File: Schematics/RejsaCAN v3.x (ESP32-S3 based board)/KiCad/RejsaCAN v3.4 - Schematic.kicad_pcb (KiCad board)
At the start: 4 copper layers, 63 x 49.5 mm, 86 parts, among them J1 Micro-Fit 3.0 4P R/A, J2 U.FL, J3 JST-XH 4P LTE, Q1 SS8050, U1 ESP32-S3-WROOM-1(N16R8), U2 SN65HVD230DR, U3 ME2807A33M3G, U4 LMR14006XDDCR, U5 MT9700, U6 CPC1018N, U7 LG290P03AAMD, U8 AP2112K-3.3

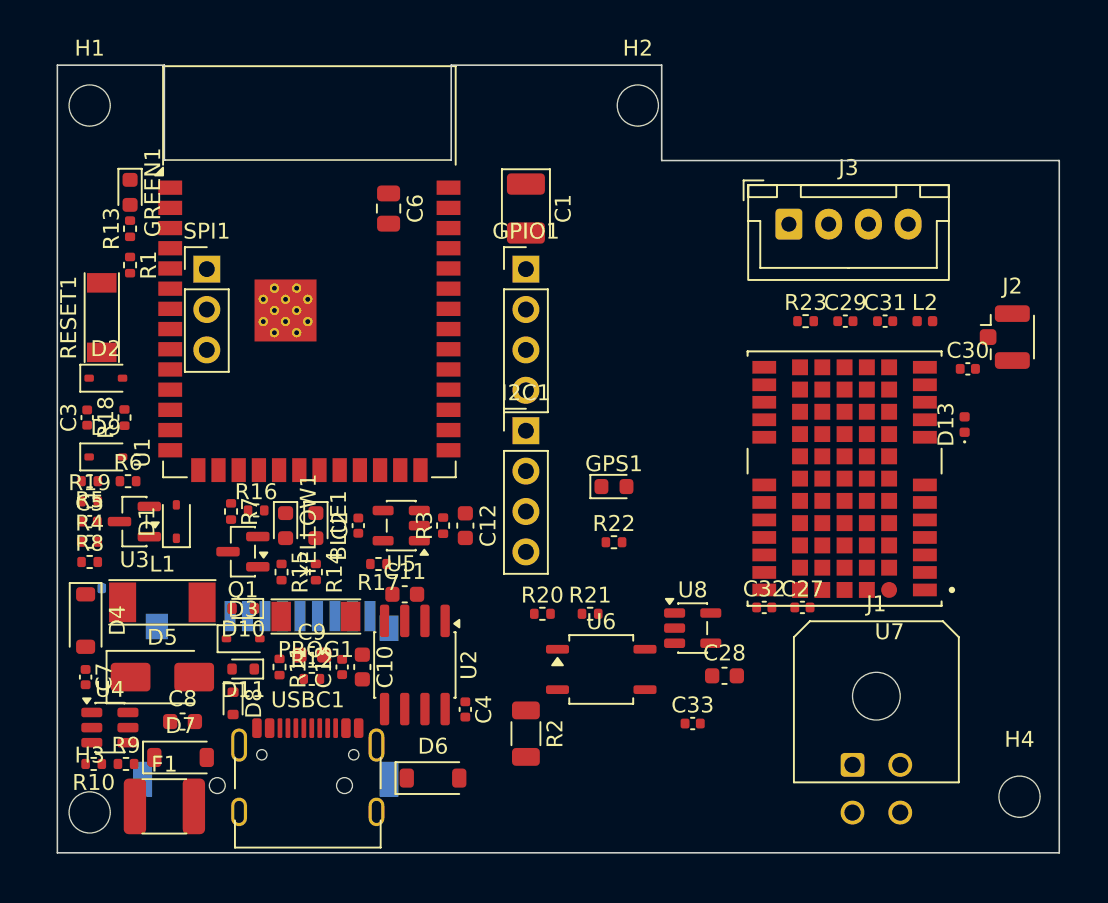
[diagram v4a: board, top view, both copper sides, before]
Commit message: Route the v3.5 board: 882 tracks, 85 vias, GND poured on three layers
DRC is clean of every electrical and fabrication class -- no shorts, no
clearance violations, no crossings, no solder-mask bridges, no starved
thermals, no annular-ring or board-edge errors. Five connections remain
open, all in the power corner; finish them in the GUI's interactive
router, which can shove existing traces where the Python API cannot.

  F.Cu       813.7 mm
  PWR_plane  762.1 mm
  B.Cu       296.4 mm
  GND_plane  0 mm  -- held solid on purpose

Routing took three Freerouting runs and the first two taught us things.

Run 1 (12 unrouted): I had raised the Battery net class to 0.8mm wide
and 0.6mm clearance, quoting IPC-2221 at 31-50V. Six of the twelve
failures were VCC and all twelve sat in the power corner. That 0.6mm is
table B2, for UNCOATED external conductors. A soldermasked board is
table B4, which asks 0.13mm. The original 0.35mm was already 2.7x the
requirement, so the change bought nothing and cost the corner. Reverted
to 0.6/0.35, and VBAT_IN split into its own Battery_Out class at 0.8mm
since it feeds the LTE module and lives in the roomy bump-out.

Run 2 (4 unrouted): better, but KiCad exports every copper layer as
(type signal), so the router put 560mm of traces on In1 -- the layer
meant to be the solid reference under the antenna. Editing the DSN to
(type power) holds it as a plane; Freerouting accepts that and routes
the other three layers.

Run 3 (5 unrouted) is what shipped: one more open connection than run 2
in exchange for an intact ground plane, which is the right trade.

The antenna path is hand-routed, not autorouted. Freerouting had taken
GNSS_ANT through two vias down to B.Cu and necked GNSS_RF_IN to 0.225mm
against the 0.30mm class width -- both change the impedance. It is now
12.4mm total on F.Cu only, constant 0.30mm, zero vias, with the inner
plane verified clear of foreign copper beneath it. C30 was flipped so
the DC block sits inline instead of forcing 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
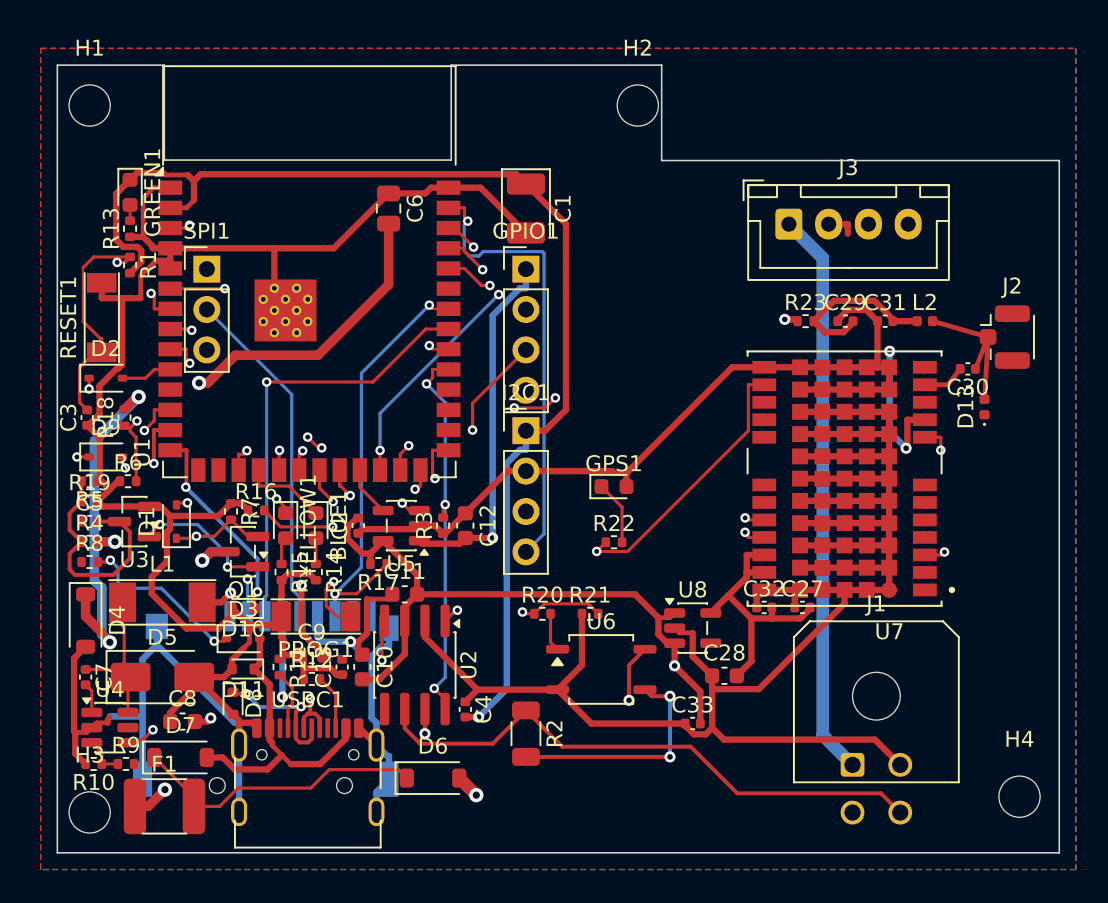
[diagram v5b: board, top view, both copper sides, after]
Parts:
- moved D13 1.67 mm to (168.3, 201.5)
- turned C30 to 180 degrees
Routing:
- net GND: track 0.00 -> 398.0 mm, vias 0 -> 1
- net 3V3: track 0.00 -> 173.0 mm, vias 0 -> 6
- net USB_D+: track 0.00 -> 95.6 mm, vias 0 -> 3
- net USB_D-: track 0.00 -> 93.7 mm, vias 0 -> 3
- net VCC: track 0.00 -> 73.9 mm, vias 0 -> 6
- net VBAT_IN: track 0.00 -> 61.6 mm, vias 0 -> 1
- net GPIO7: track 0.00 -> 61.2 mm, vias 0 -> 2
- net GPIO6: track 0.00 -> 57.9 mm, vias 0 -> 4
- net MTDI: track 0.00 -> 51.6 mm, vias 0 -> 2
- net GPS_LOCK: track 0.00 -> 50.4 mm, vias 0 -> 4
- net MTCK: track 0.00 -> 44.6 mm, vias 0 -> 1
- net CAN_H: track 0.00 -> 40.1 mm, vias 0 -> 2
- net TERM_EN: track 0.00 -> 37.5 mm, vias 0 -> 2
- net MTDO: track 0.00 -> 36.3 mm, vias 0 -> 1
- net CAN_L: track 0.00 -> 36.3 mm
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- added copper zone on B.Cu, net GND
- added copper zone on F.Cu, net GND
- added copper zone on In1.Cu, net GND

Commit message: Act on the design-rule audit: antenna keepout, input trace, RF stubs
A 7-agent audit checked this board's rules against published sources and
probed the board file. It found things that would have shipped.

A8 -- MY DEFECT, the serious one. Going to 4 layers did not extend the
antenna keep-outs, which still listed F.Cu/B.Cu from the 2-layer era, so
the new In1 plane flooded 97 mm2 of solid copper about 0.21 mm under the
ESP32-S3's PCB antenna. That detunes it. Keep-out now covers all four
layers; verified 0/280 sample points filled where it was solid before.

Corollary caught on the way: I first extended J2's keep-out the same way,
which was wrong. U1 is a radiating antenna and needs all-layer clearance;
J2 is a connector body needing surface clearance only, and forbidding
inner copper there deletes the ground reference under the u.FL. Reverted
to F.Cu. Two keep-outs that look alike serve opposite purposes.

A2 Net-(D6-K) had no netclass pattern at all, so it fell to Default and
routed at 0.20mm -- while carrying 100% of the input current from both
D6 and D7 into F1. IPC-2221 gives 0.20mm 1oz outer about 0.74A at dT10,
behind a fuse that HOLDS at 1.1A and trips at 2.2A: the trace was the
fuse. Now in Battery class at 0.6mm.

Q1 my IPC citation was wrong, and right by luck. Table 6-1 is indexed by
COATING, not layer. Solder-masked tracks are column B4 = 0.13mm, not B2's
0.60mm. So 0.35mm has 2.7x margin and CLAUDE.md's "raise to 0.6mm on the
respin" was chasing a column that does not apply -- it was tried here and
cost the power corner its routability for nothing. Comments corrected.

The rule that WAS wrong is pad-to-pad: an unscoped 0.15mm exception
granted every pad on the board, including bare battery-voltage ones where
column A6 asks 0.50mm. Now scoped to the U2/C11 pair it was written for,
with a new A6 rule that excludes same-package pins, since IPC governs
board conductors and not a TSOT-23's pin pitch.

Q3 the antenna stubs were real: 3.6mm and 3.9mm taps co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
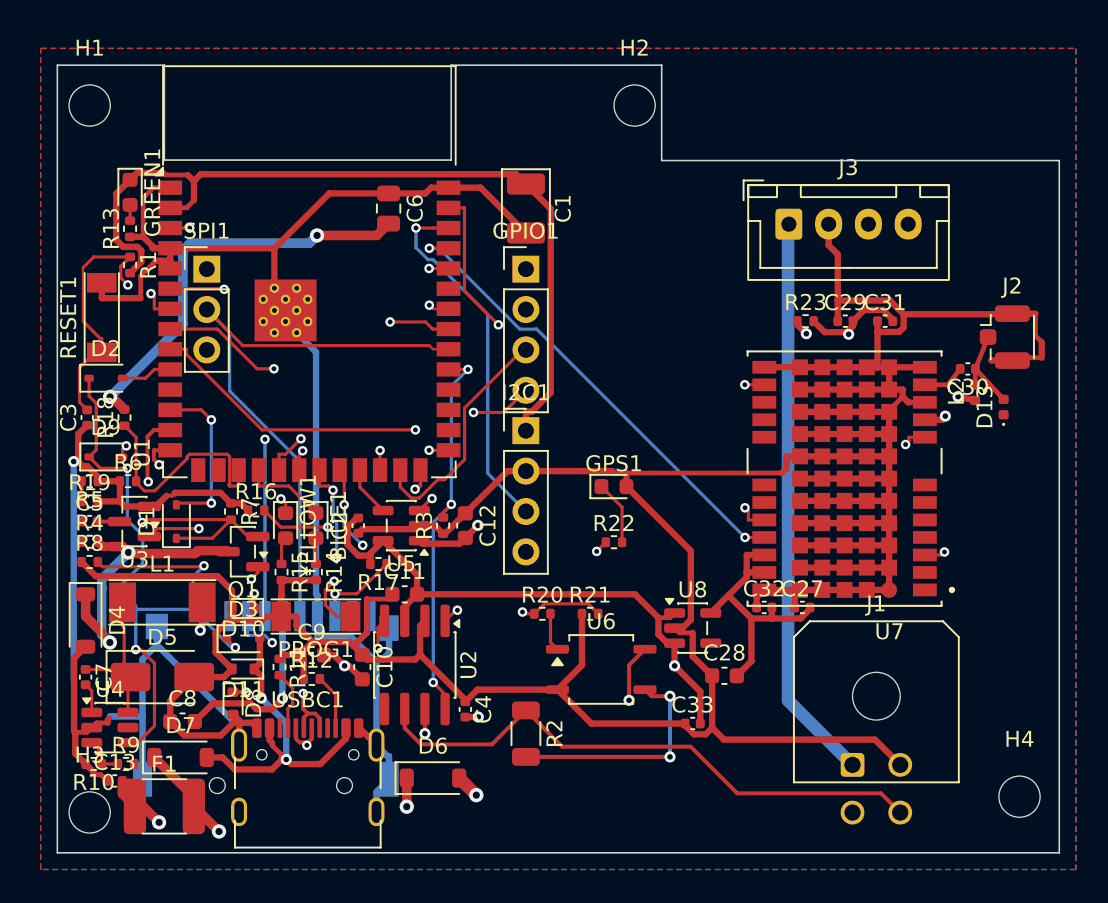
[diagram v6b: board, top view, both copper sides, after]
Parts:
- moved C13 16.0 mm to (113.6, 225.0), turned to 0 degrees
- moved L2 5.49 mm to (167.7, 200.6), turned to 90 degrees
- moved D13 1.20 mm to (169.5, 201.5)
- moved H2 0.20 mm to (146.3, 182.5)
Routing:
- net GND: track 398.0 -> 430.8 mm
- net 3V3: track 173.0 -> 158.8 mm, vias 6 -> 5
- net Net-(D2-K): track 33.5 -> 46.4 mm, vias 5 -> 4
- net MTDI: track 51.6 -> 39.4 mm
- net Net-(U3-VIN): track 14.8 -> 2.67 mm
- net GPS_LOCK: track 50.4 -> 60.1 mm, vias 4 -> 3
- net RXD: track 26.9 -> 35.8 mm
- net USB_D+: track 95.6 -> 88.4 mm
- net USB_D-: track 93.7 -> 100.4 mm
- net MTCK: track 44.6 -> 37.9 mm, vias 1 -> 0
- net GPIO12: track 24.4 -> 17.7 mm, vias 1 -> 2
- net GNSS_BIAS: track 10.7 -> 16.1 mm, vias 0 -> 2
- net CAN_TX: track 18.8 -> 14.0 mm, vias 2 -> 3
- net Net-(D1-K): track 13.1 -> 17.7 mm
- net GNSS_VDD_RF: track 17.7 -> 13.3 mm, vias 3 -> 2
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
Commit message: PCB: rebuild for the new front end, spread the power corner, re-route
DRC clean of every electrical and fabrication class. 4 connections open, all
in the power section; finish them in the GUI's interactive router, which can
shove existing traces where the Python API cannot.

  947 tracks, 80 vias, 87 footprints
  PWR_plane  875.2 mm
  F.Cu       872.7 mm
  B.Cu       267.3 mm
  GND_plane  0 mm  -- held solid as the RF reference

Smaller packages, chosen on the numbers rather than to save space:

  D4  SMB -> SMA   SMAJ33CA. The actual pulse-1 energy is 61 mJ; SMAJ's 400 W
                   is 0.4 J, a 6.5x margin. The SMB had been sized off a figure
                   the synthesis itself flagged as ~10x high (it used 24 V
                   system pulse levels on a 12 V board).
  D6  SMA -> SOD-123FL  SS110, 100 V / 1 A. D6 carries only this board's own
  D7  SMA -> SOD-123FL  draw; the LTE branch taps VBAT_IN upstream of D6 and
                   has its own fuse, so 3 A was sizing for current that never
                   flows through it.

That took the component-area delta from +47 mm2 to +9.1 mm2 and removed the
need to grow the board.

Power corner spread. 12 low-speed parts (U3, R4, R5, R19, R6, C5, D1, D2, D9,
Q1, R7, R8 -- the battery-sense divider and the auto-shutdown chain) moved out
of the congested area. U4, L1 and D5 stayed put deliberately: they are the
switching loop, and moving them would lengthen the SW node, which already sits
45 mm from a GNSS receiver.

The split is by circuit type, not geography. The sense and shutdown circuits
are high-impedance and indifferent to a few extra millimetres; the buck is not.

Effect: the router finished in 131 s against 310-660 s on every previous
attempt, and courtyard overlaps fell 43 -> 26.

Placement was searched, not hand-picked. Three earlier attempts at choosing
coordinates by eye put C13 on the feedback divider, stacked the RF parts into
each other, and read one row of a free-space map as if the block 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
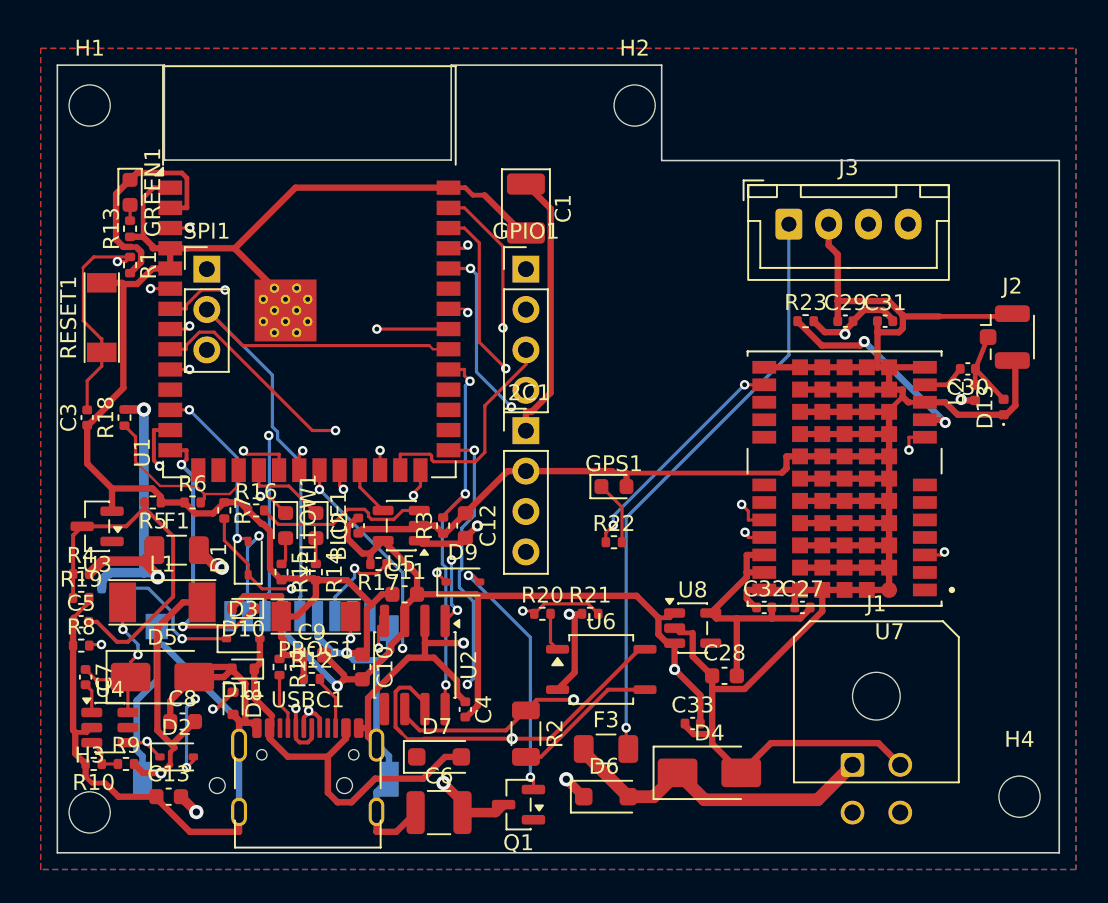
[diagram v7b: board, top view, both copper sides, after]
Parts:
- added F3: 1206TD-4A, Fuse_1206_3216Metric, F.Cu at (144.5, 223.0)
- C13: value 100nF -> 100nF/100V; footprint Capacitor_SMD:C_0402_1005Metric -> C_0603_1608Metric
- C6: value 22uF -> 2.2uF/100V; footprint Capacitor_SMD:C_0805_2012Metric -> C_1210_3225Metric
- D4: value SMF30A -> SMAJ33CA; footprint Diode_SMD:D_SOD-123 -> D_SMA
- D6, D7: value DSS34 -> SS110; footprint Diode_SMD:D_SOD-123 -> D_SOD-123F
- F1: value MF-MSMF110/16-2 -> 1206TD-2A; footprint RejsaCAN:Fuse_1812_RejsaCAN_3.706mm -> Fuse_1206_3216Metric
- moved D4 40.4 mm to (151.0, 224.5), turned to 0 degrees
- moved C6 38.1 mm to (134.0, 227.0), turned to 0 degrees
- moved D2 24.2 mm to (117.5, 223.5)
- moved D9 23.8 mm to (135.5, 212.5)
- moved Q1 23.5 mm to (139.0, 226.5)
- moved D7 16.3 mm to (134.0, 223.5)
- moved F1 16.1 mm to (117.5, 210.5)
- moved D6 10.9 mm to (144.5, 226.0)
- moved C5 6.32 mm to (111.5, 215.0)
- moved R19 6.09 mm to (111.5, 213.5)
- moved R8 5.28 mm to (111.5, 216.5)
- moved D1 5.07 mm to (122.0, 211.0)
- moved R6 4.27 mm to (118.5, 207.5)
- moved R5 4.19 mm to (116.0, 207.5)
- moved C13 3.53 mm to (117.0, 226.0)
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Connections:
- D4 pad 1: VCC -> VBAT_IN
- J3 pad 1: VBAT_IN -> J3_PWR
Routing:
- net VBAT_IN: track 61.7 -> 20.5 mm, vias 1 -> 0
- net J3_PWR: track 0.00 -> 37.3 mm, vias 0 -> 1
- net FORCE_ON: track 3.23 -> 30.7 mm, vias 0 -> 3
- net Net-(U3-VIN): track 2.67 -> 22.8 mm
- net 3V3: track 158.8 -> 140.8 mm, vias 5 -> 3
- net Net-(D1-K): track 17.7 -> 34.7 mm, vias 2 -> 3
- net GPIO12: track 17.7 -> 33.2 mm, vias 2 -> 1
- net Net-(D2-K): track 46.4 -> 58.7 mm
- net USB_D+: track 88.4 -> 99.1 mm
- net Net-(D6-K): track 21.2 -> 31.3 mm
- net PROG: track 17.9 -> 27.2 mm, vias 2 -> 3
- net Net-(Q1-B): track 8.88 -> 0.00 mm, vias 2 -> 0
- net GND: track 430.8 -> 439.3 mm, vias 1 -> 3
- net GPIO47: track 15.4 -> 23.3 mm
- net USB_D-: track 100.4 -> 108.1 mm
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
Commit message: PCB: finish routing (0 unconnected), stitch ground, clean courtyards; DRC 0 errors
Routing: the last 4 open connections are closed by a scripted obstacle-aware
grid router (per-layer clearance-inflated raster, Dijkstra over F/In2/B with
via transitions), each route accepted only when kicad-cli DRC did not rise.
- Net-(Q1-B): B.Cu down the left edge and along the bottom, 2 vias.
- 3V3 module island (U1.2/GREEN1/R1): F -> In2 under the module -> C1.
- Net-(D6-K): D7 rotated 180 so its cathode faces the free F.Cu toward the
  existing D6-K via; USB5V re-stubbed straight down onto its track.
- VCC -> U4.5: EN (Net-(D2-K)) and FORCE_ON stripped, the 3V3 F.Cu feed
  from L1.2 removed, VCC routed F.Cu-only from the pad to C13.2 (0.4 mm
  through the 0.6 mm pad exit), L1.2 -> C8.2 relinked via In2, C8.2 tied
  to the In2 3V3 diagonal, then EN (5 links) and FORCE_ON re-routed.

Ground: 98 stitching vias (0.6/0.3) - a fence both sides of the RF trace,
a ring around U7's ground pads, and a 4 mm grid - all pruned by DRC.

Courtyards: U7 (LG290P03) courtyard was 18.2x22 for a 12.2x16 module;
now 12.7x16.5 in the library and the board. C27/C32 physically sat under
the module edge; now rotated 90 side by side below it, 0.6 mm stubs to
the GNSS_VCC bus. U6/R2 nudged apart. U1's antenna rule area now forbids
copper only (tracks/vias/pour); NPTH mounting holes are not copper.

The 25 remaining courtyard-class findings are all present on the fabricated
v3.4 layout (which has 43); the three courtyard checks are now warnings,
consistent with the project's existing as-fabricated rules.

Co-Authored-By: Claude Fable 5 <noreply@anthropic.com>
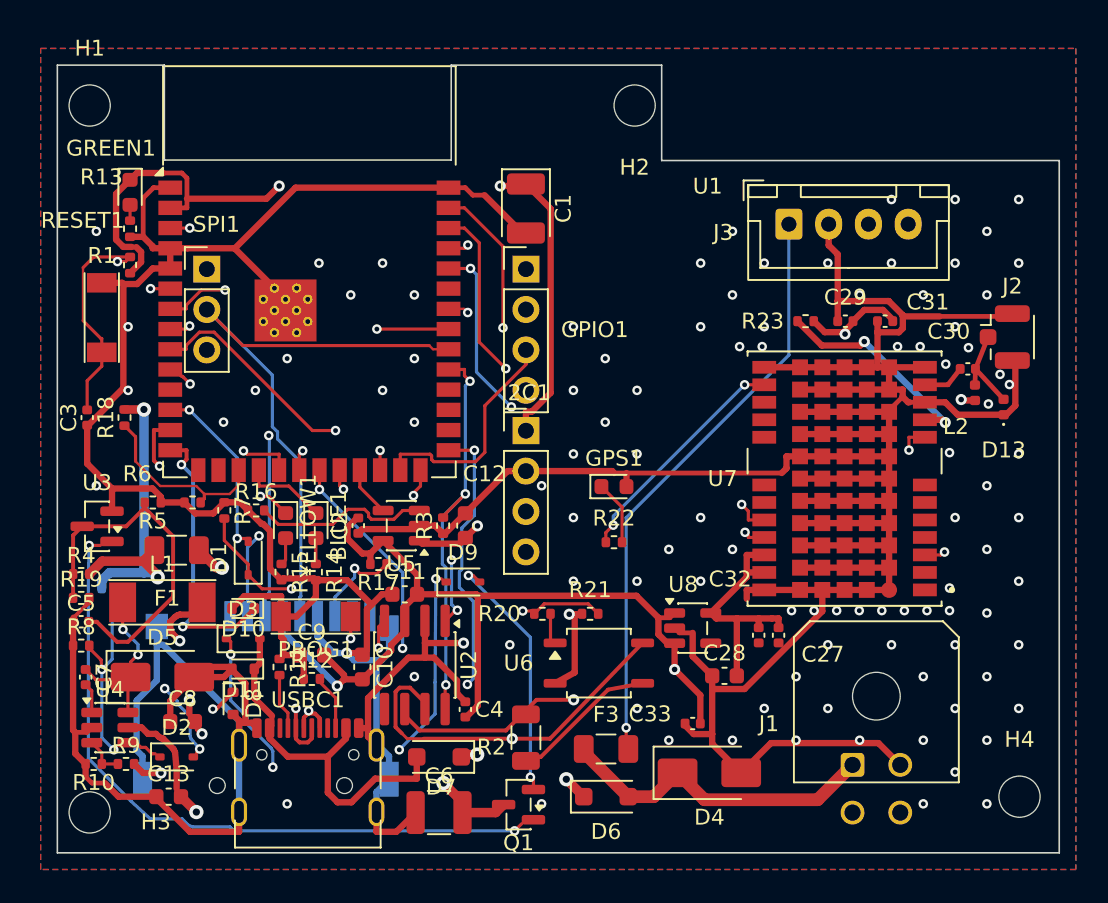
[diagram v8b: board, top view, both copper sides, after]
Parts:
- moved C27 2.30 mm to (155.3, 215.8), turned to 90 degrees
- moved C32 1.78 mm to (154.1, 215.8), turned to 90 degrees
- moved U6 0.43 mm to (144.0, 217.6)
- moved R2 0.25 mm to (139.5, 222.3)
- turned D7 to 180 degrees
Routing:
- net Net-(Q1-B): track 0.00 -> 43.3 mm, vias 0 -> 2
- net 3V3: track 140.8 -> 154.3 mm, vias 3 -> 8
- net VCC: track 69.8 -> 75.8 mm
- net Net-(D6-K): track 31.3 -> 35.5 mm, vias 2 -> 3
- net Net-(D2-K): track 58.7 -> 55.5 mm, vias 4 -> 6
- net FORCE_ON: track 30.7 -> 28.0 mm
- net GND: track 439.3 -> 437.3 mm, vias 3 -> 101
- net USB5V: track 25.4 -> 23.4 mm
- net GNSS_VCC: track 17.8 -> 16.0 mm
